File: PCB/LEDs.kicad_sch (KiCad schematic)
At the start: 4 parts, among them J2 Display

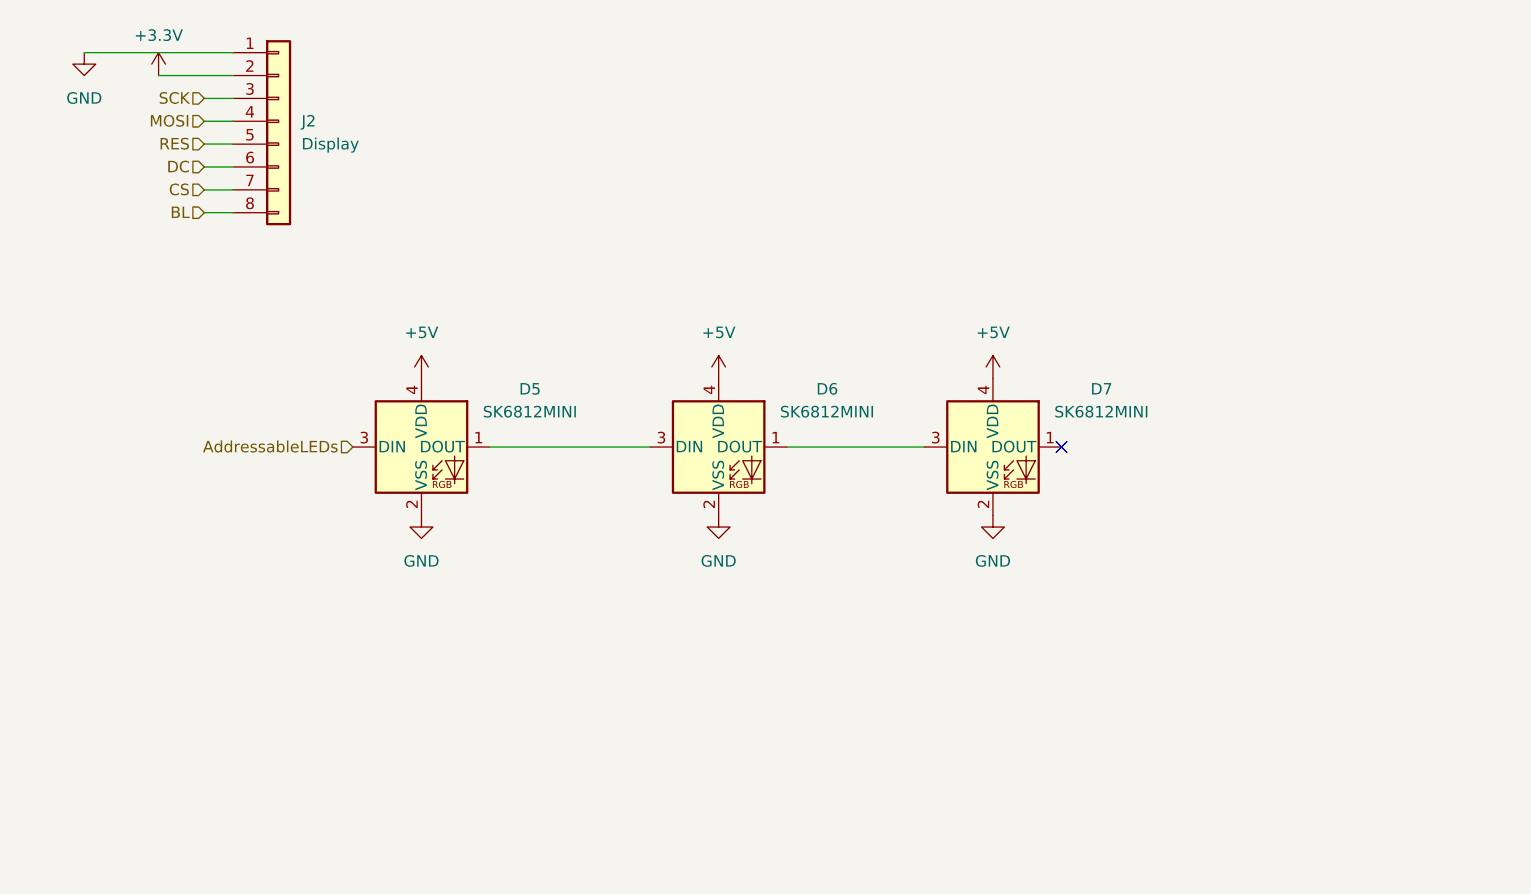
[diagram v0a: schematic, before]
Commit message: only need to find boot and reset footprints
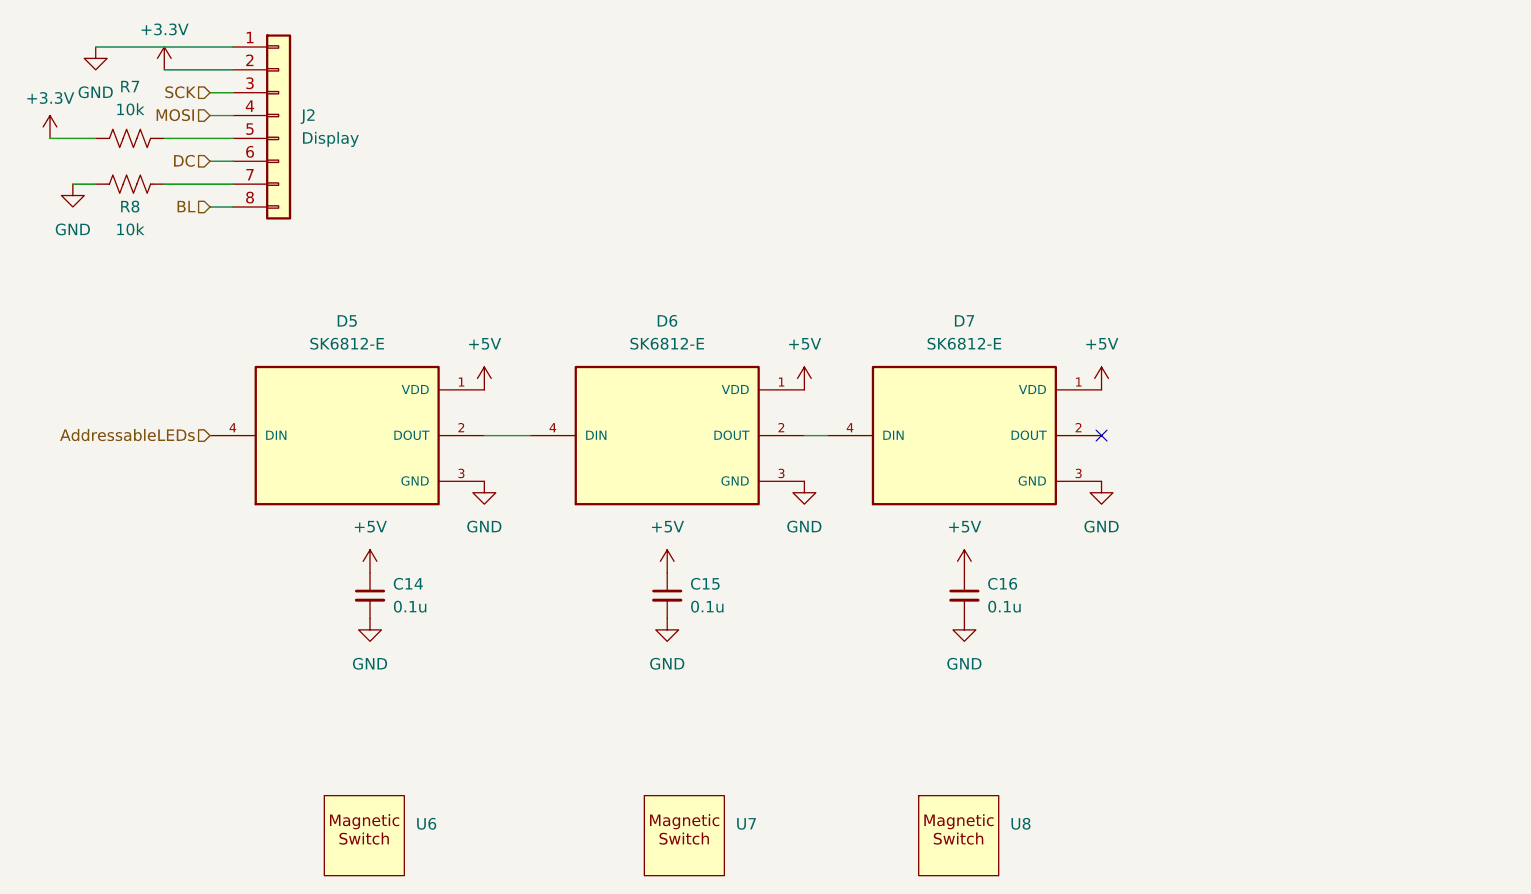
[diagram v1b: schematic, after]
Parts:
- removed D5, D6, D7: SK6812MINI, LED_SMD:LED_SK6812MINI_PLCC4_3.5x3.5mm_P1.75mm, symbol LED:SK6812MINI
- added C14, C15, C16: 0.1u, Capacitor_SMD:C_0603_1608Metric_Pad1.08x0.95mm_HandSolder, symbol Device:C_Small
- added D5, D6, D7: SK6812-E, SK6812MINI-E:LED_SK6812-E, symbol SK6812MINI-E:SK6812-E
- added R7, R8: 10k, Resistor_SMD:R_0603_1608Metric_Pad0.98x0.95mm_HandSolder, symbol Device:R_US
- added U6, U7, U8: ~, Magnetic Axis Switch:Cherry MX compatible, symbol Magnetic Axis Switch:Magnetic_Axis_Switch
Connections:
- net +3.3V: now also R7.1
- net +5V: now also C14.1, C15.1, C16.1, D5.1 (VDD), D6.1 (VDD), D7.1 (VDD)
- net AddressableLEDs: now also D5.4 (DIN)
- net GND: now also C14.2, C15.2, C16.2, D5.3 (GND), D6.3 (GND), D7.3 (GND), R8.1
- net CS: no longer names the net of J2.7 (Pin_7)
- net CS: now also R8.2
- net RES: no longer names the net of J2.5 (Pin_5)
- net RES: now also R7.2
- new net: D6.2 (DOUT), D7.4 (DIN)
- new net: D5.2 (DOUT), D6.4 (DIN)
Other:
- moved on the sheet: J2

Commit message: changing to wasd
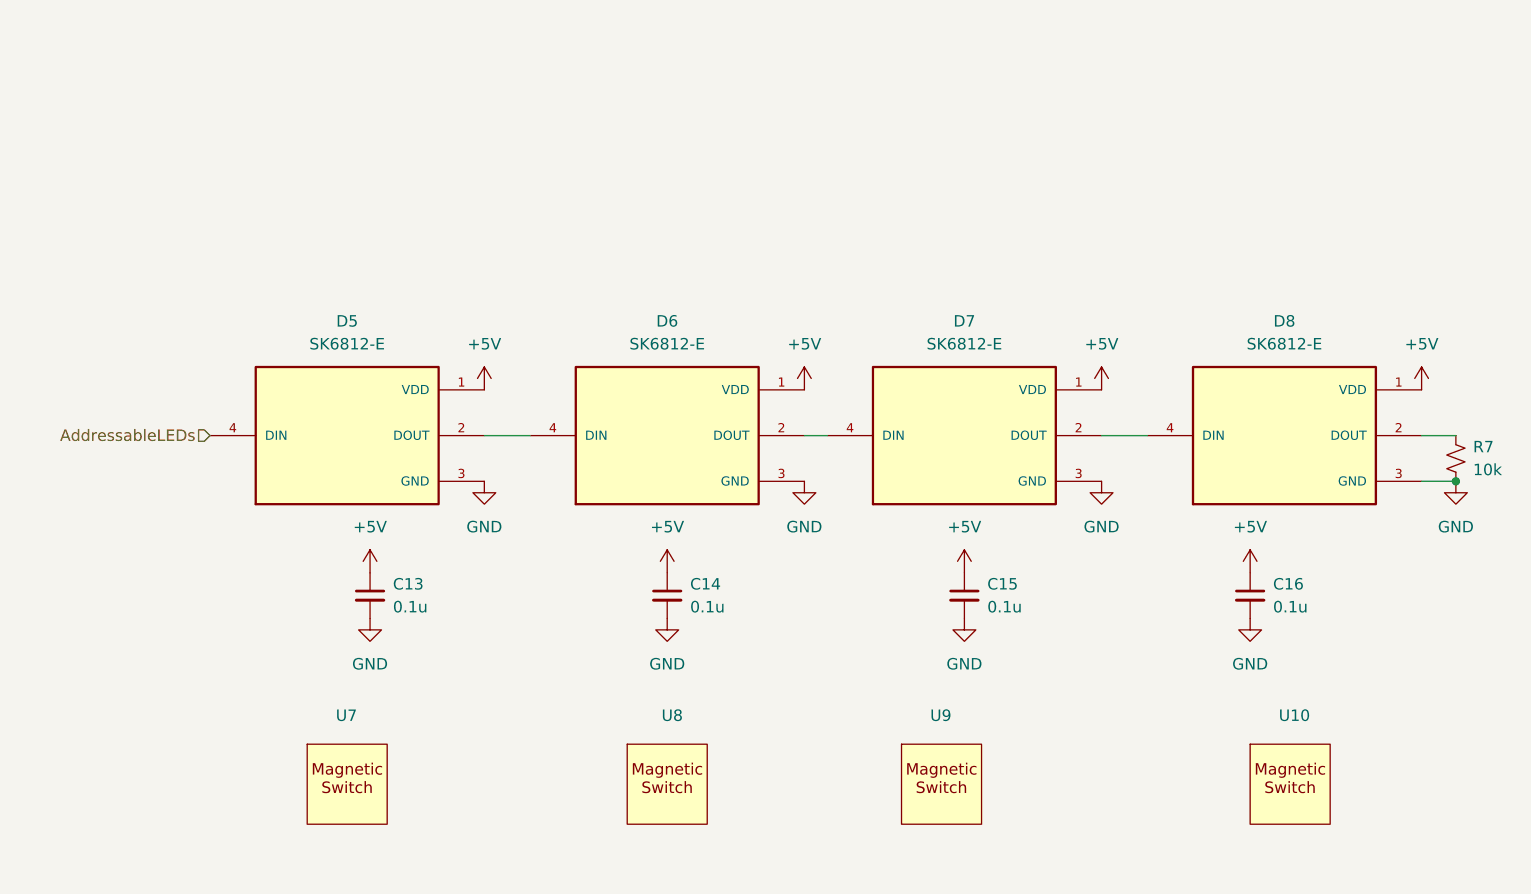
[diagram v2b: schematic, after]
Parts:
- removed J2: Display, Connector_PinHeader_2.54mm:PinHeader_1x08_P2.54mm_Vertical, symbol Connector_Generic:Conn_01x08
- removed R7, R8: 10k, Resistor_SMD:R_0603_1608Metric_Pad0.98x0.95mm_HandSolder, symbol Device:R_US
- added C16: 0.1u, Capacitor_SMD:C_0603_1608Metric_Pad1.08x0.95mm_HandSolder, symbol Device:C_Small
- added D8: SK6812-E, SK6812MINI-E:LED_SK6812-E, symbol SK6812MINI-E:SK6812-E
- added R7: 10k, Resistor_SMD:R_0603_1608Metric_Pad0.98x0.95mm_HandSolder, symbol Device:R_Small_US
- added U10: ~, Magnetic Axis Switch:Cherry MX compatible, symbol Magnetic Axis Switch:Magnetic_Axis_Switch
- renumbered C14 to C13, C15 to C14, C16 to C15, U6 to U7, U7 to U8, U8 to U9
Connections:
- net +5V: now also C16.1, D8.1 (VDD)
- net GND: now also C16.2, D8.3 (GND), R7.2
- net at D7.2 (DOUT): now also D8.4 (DIN)
- new net: D8.2 (DOUT), R7.1
- no-connect marks 1 -> 0
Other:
- moved on the sheet: U7, U8, U9

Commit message: new update
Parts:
- renumbered C13 to C17, C14 to C18, C15 to C19, C16 to C20
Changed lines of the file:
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@@
 		(dnp no)
 		(fields_autoplaced yes)
-		(property "Reference" "#PWR045"
+		(property "Reference" "#PWR053"
 			(at 86.36 80.01 0)
 			(effects
@@
 			(project ""
 				(path "/f410b0a0-725c-464e-80be-c0074224226d/7f2ee157-0544-4b4f-a393-7ad097fd1635"
-					(reference "#PWR045")
+					(reference "#PWR053")
 					(unit 1)
 				)
@@
 		(dnp no)
 		(fields_autoplaced yes)
-		(property "Reference" "#PWR047"
+		(property "Reference" "#PWR055"
 			(at 106.68 95.25 0)
 			(effects
@@
 			(project "OTCboard"
 				(path "/f410b0a0-725c-464e-80be-c0074224226d/7f2ee157-0544-4b4f-a393-7ad097fd1635"
-					(reference "#PWR047")
+					(reference "#PWR055")
 					(unit 1)
 				)
@@
 		(dnp no)
 		(fields_autoplaced yes)
-		(property "Reference" "#PWR053"
+		(property "Reference" "#PWR061"
 			(at 154.94 80.01 0)
 			(effects
@@
 			(project "OTCboard"
 				(path "/f410b0a0-725c-464e-80be-c0074224226d/7f2ee157-0544-4b4f-a393-7ad097fd1635"
-					(reference "#PWR053")
+					(reference "#PWR061")
 					(unit 1)
 				)
@@
 		(dnp no)
 		(fields_autoplaced yes)
-		(property "Reference" "#PWR050"
+		(property "Reference" "#PWR058"
 			(at 139.7 87.63 0)
 			(effects
@@
 			(project "OTCboard"
 				(path "/f410b0a0-725c-464e-80be-c0074224226d/7f2ee157-0544-4b4f-a393-7ad097fd1635"
-					(reference "#PWR050")
+					(reference "#PWR058")
 					(unit 1)
 				)
@@
 		(dnp no)
 		(fields_autoplaced yes)
-		(property "Reference" "C16"
+		(property "Reference" "C20"
 			(at 173.99 85.0962 0)
 			(effects
@@
 			(project "OTCboard"
 				(path "/f410b0a0-725c-464e-80be-c0074224226d/7f2ee157-0544-4b4f-a393-7ad097fd1635"
-					(reference "C16")
+					(reference "C20")
 					(unit 1)
 				)
@@
 		(dnp no)
 		(fields_autoplaced yes)
-		(property "Reference" "#PWR049"
+		(property "Reference" "#PWR057"
 			(at 121.92 80.01 0)
 			(effects
@@
 			(project "OTCboard"
 				(path "/f410b0a0-725c-464e-80be-c0074224226d/7f2ee157-0544-4b4f-a393-7ad097fd1635"
-					(reference "#PWR049")
+					(reference "#PWR057")
 					(unit 1)
 				)
@@
 		(dnp no)
 		(fields_autoplaced yes)
-		(property "Reference" "#PWR048"
+		(property "Reference" "#PWR056"
 			(at 121.92 67.31 0)
 			(effects
@@
 			(project "OTCboard"
 				(path "/f410b0a0-725c-464e-80be-c0074224226d/7f2ee157-0544-4b4f-a393-7ad097fd1635"
-					(reference "#PWR048")
+					(reference "#PWR056")
 					(unit 1)
 				)
@@
 		(dnp no)
 		(fields_autoplaced yes)
-		(property "Reference" "#PWR052"
+		(property "Reference" "#PWR060"
 			(at 154.94 67.31 0)
 			(effects
@@
 			(project "OTCboard"
 				(path "/f410b0a0-725c-464e-80be-c0074224226d/7f2ee157-0544-4b4f-a393-7ad097fd1635"
-					(reference "#PWR052")
+					(reference "#PWR060")
 					(unit 1)
 				)
@@
 		(dnp no)
 		(fields_autoplaced yes)
-		(property "Reference" "#PWR056"
+		(property "Reference" "#PWR064"
 			(at 190.5 67.31 0)
 			(effects
@@
 			(project "OTCboard"
 				(path "/f410b0a0-725c-464e-80be-c0074224226d/7f2ee157-0544-4b4f-a393-7ad097fd1635"
-					(reference "#PWR056")
+					(reference "#PWR064")
 					(unit 1)
 				)
@@
 		(dnp no)
 		(fields_autoplaced yes)
-		(property "Reference" "#PWR046"
+		(property "Reference" "#PWR054"
 			(at 106.68 87.63 0)
 			(effects
@@
 			(project "OTCboard"
 				(path "/f410b0a0-725c-464e-80be-c0074224226d/7f2ee157-0544-4b4f-a393-7ad097fd1635"
-					(reference "#PWR046")
+					(reference "#PWR054")
 					(unit 1)
 				)
@@
 		(dnp no)
 		(fields_autoplaced yes)
-		(property "Reference" "C14"
+		(property "Reference" "C18"
 			(at 109.22 85.0962 0)
 			(effects
@@
 			(project "OTCboard"
 				(path "/f410b0a0-725c-464e-80be-c0074224226d/7f2ee157-0544-4b4f-a393-7ad097fd1635"
-					(reference "C14")
+					(reference "C18")
 					(unit 1)
 				)
@@
 		(dnp no)
 		(fields_autoplaced yes)
-		(property "Reference" "#PWR042"
+		(property "Reference" "#PWR050"
 			(at 73.66 87.63 0)
 			(effects
@@
 			(project "OTCboard"
 				(path "/f410b0a0-725c-464e-80be-c0074224226d/7f2ee157-0544-4b4f-a393-7ad097fd1635"
-					(reference "#PWR042")
+					(reference "#PWR050")
 					(unit 1)
 				)
@@
 		(dnp no)
 		(fields_autoplaced yes)
-		(property "Reference" "#PWR055"
+		(property "Reference" "#PWR063"
 			(at 171.45 95.25 0)
 			(effects
@@
 			(project "OTCboard"
 				(path "/f410b0a0-725c-464e-80be-c0074224226d/7f2ee157-0544-4b4f-a393-7ad097fd1635"
-					(reference "#PWR055")
+					(reference "#PWR063")
 					(unit 1)
 				)
@@
 		(dnp no)
 		(fields_autoplaced yes)
-		(property "Reference" "#PWR057"
+		(property "Reference" "#PWR065"
 			(at 194.31 80.01 0)
 			(effects
@@
 			(project "OTCboard"
 				(path "/f410b0a0-725c-464e-80be-c0074224226d/7f2ee157-0544-4b4f-a393-7ad097fd1635"
-					(reference "#PWR057")
+					(reference "#PWR065")
 					(unit 1)
 				)
@@
 		(dnp no)
 		(fields_autoplaced yes)
-		(property "Reference" "C15"
+		(property "Reference" "C19"
 			(at 142.24 85.0962 0)
 			(effects
@@
 			(project "OTCboard"
 				(path "/f410b0a0-725c-464e-80be-c0074224226d/7f2ee157-0544-4b4f-a393-7ad097fd1635"
-					(reference "C15")
+					(reference "C19")
 					(unit 1)
 				)
@@
 		(dnp no)
 		(fields_autoplaced yes)
-		(property "Reference" "#PWR043"
+		(property "Reference" "#PWR051"
 			(at 73.66 95.25 0)
 			(effects
@@
 			(project "OTCboard"
 				(path "/f410b0a0-725c-464e-80be-c0074224226d/7f2ee157-0544-4b4f-a393-7ad097fd1635"
-					(reference "#PWR043")
+					(reference "#PWR051")
 					(unit 1)
 				)
@@
 		(dnp no)
 		(fields_autoplaced yes)
-		(property "Reference" "#PWR054"
+		(property "Reference" "#PWR062"
 			(at 171.45 87.63 0)
 			(effects
@@
 			(project "OTCboard"
 				(path "/f410b0a0-725c-464e-80be-c0074224226d/7f2ee157-0544-4b4f-a393-7ad097fd1635"
-					(reference "#PWR054")
+					(reference "#PWR062")
 					(unit 1)
 				)
@@
 		(dnp no)
 		(fields_autoplaced yes)
-		(property "Reference" "#PWR044"
+		(property "Reference" "#PWR052"
 			(at 86.36 67.31 0)
 			(effects
@@
 			(project ""
 				(path "/f410b0a0-725c-464e-80be-c0074224226d/7f2ee157-0544-4b4f-a393-7ad097fd1635"
-					(reference "#PWR044")
+					(reference "#PWR052")
 					(unit 1)
 				)
@@
 		(dnp no)
 		(fields_autoplaced yes)
-		(property "Reference" "C13"
+		(property "Reference" "C17"
 			(at 76.2 85.0962 0)
 			(effects
@@
 			(project ""
 				(path "/f410b0a0-725c-464e-80be-c0074224226d/7f2ee157-0544-4b4f-a393-7ad097fd1635"
-					(reference "C13")
+					(reference "C17")
 					(unit 1)
 				)
@@
 		(dnp no)
 		(fields_autoplaced yes)
-		(property "Reference" "#PWR051"
+		(property "Reference" "#PWR059"
 			(at 139.7 95.25 0)
 			(effects
@@
 			(project "OTCboard"
 				(path "/f410b0a0-725c-464e-80be-c0074224226d/7f2ee157-0544-4b4f-a393-7ad097fd1635"
-					(reference "#PWR051")
-					(unit 1)
-				)
+					(reference "#PWR059")
+					(unit 1)
+				)
